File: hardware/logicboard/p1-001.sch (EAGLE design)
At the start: 27 parts, among them IC1 74LS07N

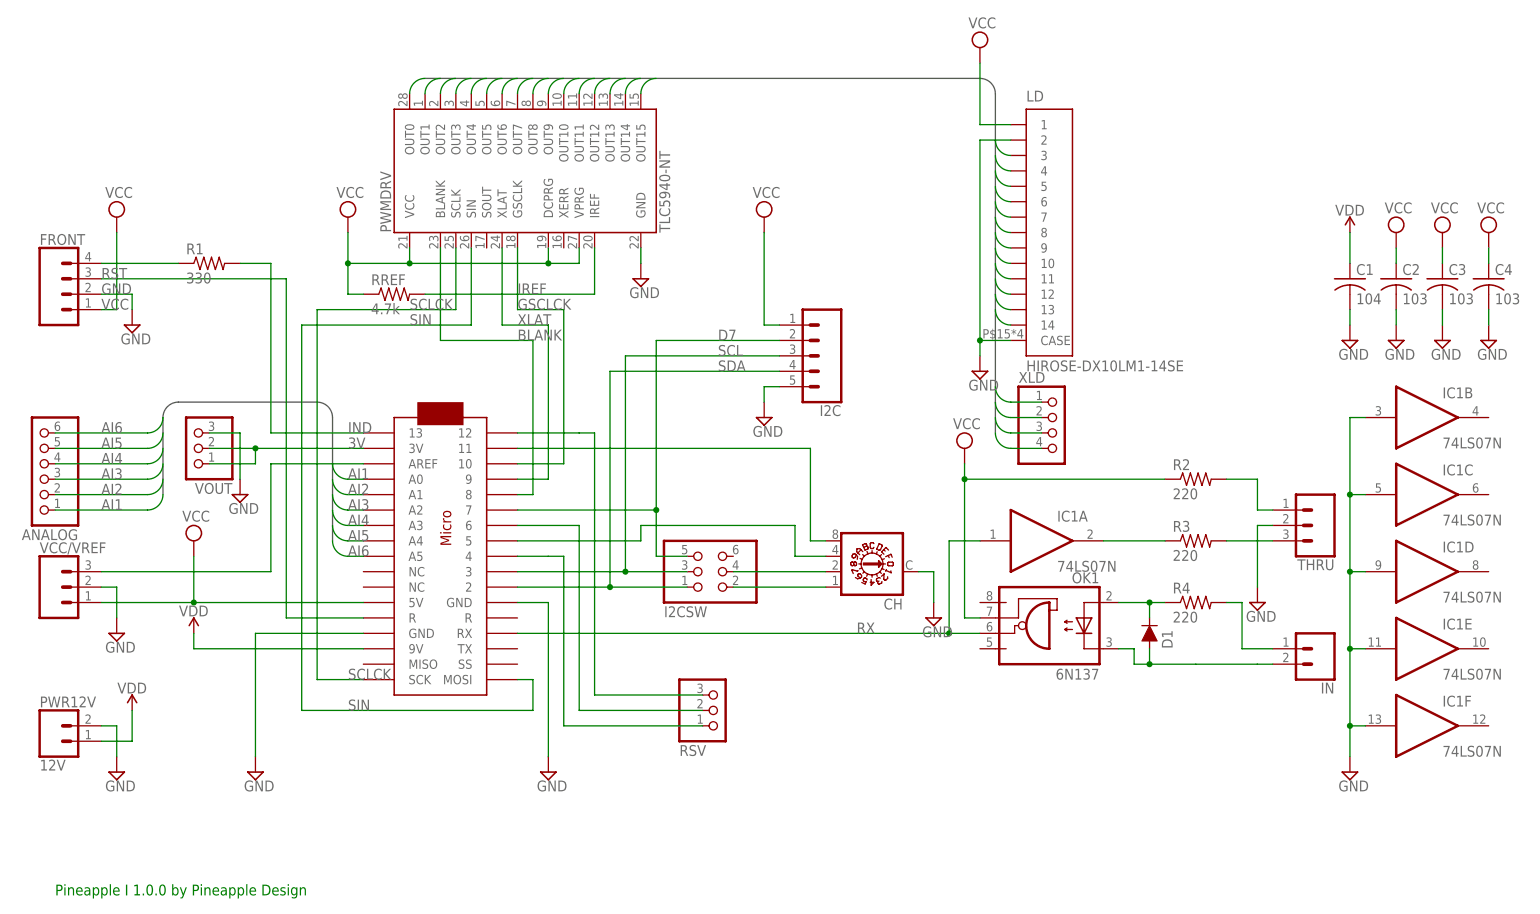
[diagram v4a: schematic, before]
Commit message: I2C pull-up.
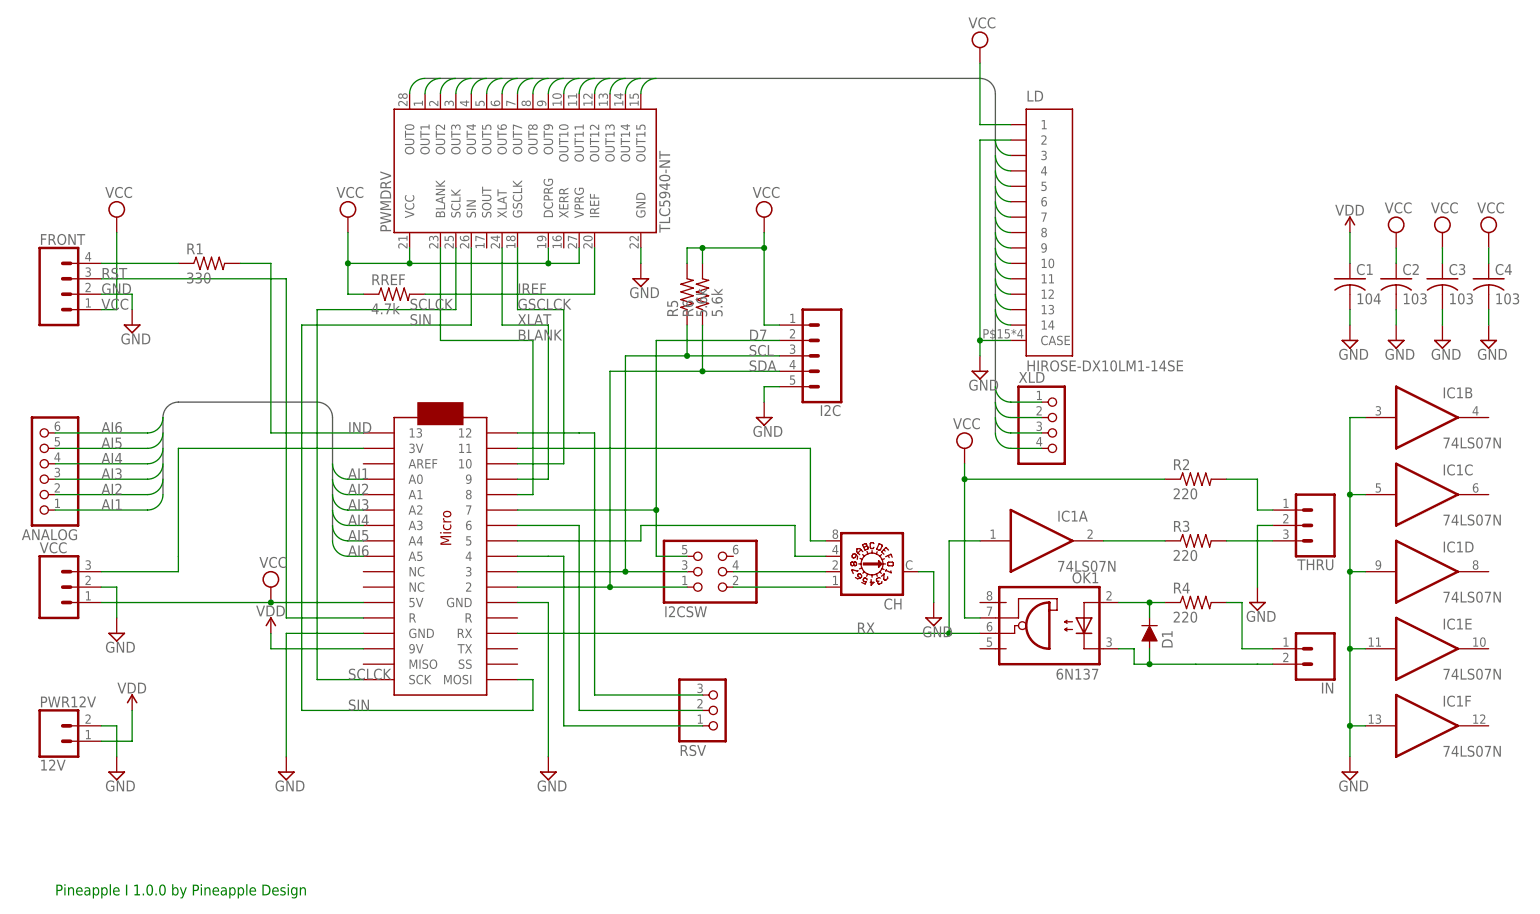
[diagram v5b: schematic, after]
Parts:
- removed VOUT: (no value), pinhead:PINHD-1X3
- added R5, R6: 5.6k, resistor:R-US_0204/5
- renumbered VCC/VREF to VCC
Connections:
- removed net 3V: U$1.3V, VOUT.1, VOUT.2
- removed net VREF: U$1.AREF, VCC.3
- new net V3V: U$1.3V, VCC.3
- net GND: no longer VOUT.3
- net SCL: now also R5.1
- net SDA: now also R6.1
- net VCC: now also R5.2, R6.2
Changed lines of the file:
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@@
 <setting verticaltext="up"/>
 </settings>
-<grid distance="0.1" unitdist="inch" unit="inch" style="lines" multiple="1" display="no" altdistance="0.01" altunitdist="inch" altunit="inch"/>
+<grid distance="0.1" unitdist="inch" unit="inch" style="dots" multiple="1" display="yes" altdistance="0.01" altunitdist="inch" altunit="inch"/>
 <layers>
 <layer number="1" name="Top" color="4" fill="1" visible="no" active="no"/>
@@
 <part name="SUPPLY8" library="supply2" library_urn="urn:adsk.eagle:library:372" deviceset="VCC" device=""/>
 <part name="SUPPLY15" library="supply2" library_urn="urn:adsk.eagle:library:372" deviceset="GND" device=""/>
-<part name="VOUT" library="pinhead" library_urn="urn:adsk.eagle:library:325" deviceset="PINHD-1X3" device="" package3d_urn="urn:adsk.eagle:package:22458/2"/>
-<part name="$1_39_$_2018-07-15_07-03-01" library="supply2" library_urn="urn:adsk.eagle:library:372" deviceset="GND" device=""/>
-<part name="VCC/VREF" library="SparkFun-Connectors" library_urn="urn:adsk.eagle:library:513" deviceset="CONN_03" device="JST-PTH-VERT" package3d_urn="urn:adsk.eagle:package:38080/1"/>
+<part name="VCC" library="SparkFun-Connectors" library_urn="urn:adsk.eagle:library:513" deviceset="CONN_03" device="JST-PTH-VERT" package3d_urn="urn:adsk.eagle:package:38080/1"/>
 <part name="$1_52_$_2018-07-15_07-03-01" library="supply2" library_urn="urn:adsk.eagle:library:372" deviceset="GND" device=""/>
+<part name="R5" library="resistor" library_urn="urn:adsk.eagle:library:348" deviceset="R-US_" device="0204/5" package3d_urn="urn:adsk.eagle:package:25955/1" value="5.6k"/>
+<part name="R6" library="resistor" library_urn="urn:adsk.eagle:library:348" deviceset="R-US_" device="0204/5" package3d_urn="urn:adsk.eagle:package:25955/1" value="5.6k"/>
 </parts>
 <sheets>
@@
 <instance part="IC1" gate="C" x="226.06" y="66.04"/>
 <instance part="D1" gate="G$1" x="180.34" y="43.18" rot="MR90"/>
-<instance part="SUPPLY14" gate="G$1" x="22.86" y="58.42"/>
-<instance part="$1_39_$_2018-07-15_07-03-06" gate="GND" x="33.02" y="20.32"/>
+<instance part="SUPPLY14" gate="G$1" x="35.56" y="50.8"/>
+<instance part="$1_39_$_2018-07-15_07-03-06" gate="GND" x="38.1" y="20.32"/>
 <instance part="IN" gate="G$1" x="208.28" y="40.64" rot="R180"/>
 <instance part="THRU" gate="J$1" x="208.28" y="60.96" rot="R180"/>
@@
 <instance part="PWR12V" gate="G$1" x="0" y="25.4"/>
 <instance part="$1_51_$_2018-07-15_07-03-06" gate="VDD" x="12.7" y="30.48"/>
-<instance part="SUPPLY12" gate="VDD" x="22.86" y="43.18"/>
+<instance part="SUPPLY12" gate="VDD" x="35.56" y="43.18"/>
 <instance part="$1_52_$_2018-07-15_07-03-06" gate="GND" x="10.16" y="20.32"/>
 <instance part="FRONT" gate="G$1" x="2.54" y="99.06"/>
@@
 <instance part="SUPPLY8" gate="G$1" x="116.84" y="111.76"/>
 <instance part="SUPPLY15" gate="GND" x="116.84" y="78.74"/>
-<instance part="VOUT" gate="A" x="22.86" y="73.66" rot="R180"/>
-<instance part="$1_39_$_2018-07-15_07-03-01" gate="GND" x="30.48" y="66.04"/>
-<instance part="VCC/VREF" gate="J$1" x="0" y="50.8"/>
+<instance part="VCC" gate="J$1" x="0" y="50.8"/>
 <instance part="$1_52_$_2018-07-15_07-03-01" gate="GND" x="10.16" y="43.18"/>
+<instance part="R5" gate="G$1" x="104.14" y="99.06" rot="R90"/>
+<instance part="R6" gate="G$1" x="106.68" y="99.06" rot="R90"/>
 </instances>
 <busses>
@@
 </segment>
 <segment>
-<wire x1="50.8" y1="43.18" x2="33.02" y2="43.18" width="0.1524" layer="91"/>
+<wire x1="50.8" y1="43.18" x2="38.1" y2="43.18" width="0.1524" layer="91"/>
 <pinref part="$1_39_$_2018-07-15_07-03-06" gate="GND" pin="GND"/>
-<wire x1="33.02" y1="43.18" x2="33.02" y2="22.86" width="0.1524" layer="91"/>
+<wire x1="38.1" y1="43.18" x2="38.1" y2="22.86" width="0.1524" layer="91"/>
 <pinref part="U$1" gate="G$1" pin="GND"/>
 </segment>
@@
 </segment>
 <segment>
-<pinref part="VOUT" gate="A" pin="3"/>
-<wire x1="25.4" y1="76.2" x2="30.48" y2="76.2" width="0.1524" layer="91"/>
-<pinref part="$1_39_$_2018-07-15_07-03-01" gate="GND" pin="GND"/>
-<wire x1="30.48" y1="76.2" x2="30.48" y2="68.58" width="0.1524" layer="91"/>
-</segment>
-<segment>
-<pinref part="VCC/VREF" gate="J$1" pin="2"/>
+<pinref part="VCC" gate="J$1" pin="2"/>
 <wire x1="7.62" y1="50.8" x2="10.16" y2="50.8" width="0.1524" layer="91"/>
 <pinref part="$1_52_$_2018-07-15_07-03-01" gate="GND" pin="GND"/>
@@
 <segment>
 <pinref part="SUPPLY14" gate="G$1" pin="VCC"/>
-<wire x1="22.86" y1="55.88" x2="22.86" y2="48.26" width="0.1524" layer="91"/>
 <pinref part="U$1" gate="G$1" pin="5V"/>
-<wire x1="22.86" y1="48.26" x2="50.8" y2="48.26" width="0.1524" layer="91"/>
-<pinref part="VCC/VREF" gate="J$1" pin="1"/>
-<wire x1="22.86" y1="48.26" x2="7.62" y2="48.26" width="0.1524" layer="91"/>
-<junction x="22.86" y="48.26"/>
+<wire x1="35.56" y1="48.26" x2="50.8" y2="48.26" width="0.1524" layer="91"/>
+<pinref part="VCC" gate="J$1" pin="1"/>
+<wire x1="35.56" y1="48.26" x2="7.62" y2="48.26" width="0.1524" layer="91"/>
+<junction x="35.56" y="48.26"/>
 </segment>
 <segment>
@@
 <segment>
 <pinref part="SUPPLY8" gate="G$1" pin="VCC"/>
-<wire x1="116.84" y1="109.22" x2="116.84" y2="93.98" width="0.1524" layer="91"/>
+<wire x1="116.84" y1="109.22" x2="116.84" y2="106.68" width="0.1524" layer="91"/>
 <pinref part="I2C" gate="G$1" pin="1"/>
+<wire x1="116.84" y1="106.68" x2="116.84" y2="93.98" width="0.1524" layer="91"/>
 <wire x1="116.84" y1="93.98" x2="119.38" y2="93.98" width="0.1524" layer="91"/>
+<pinref part="R5" gate="G$1" pin="2"/>
+<wire x1="104.14" y1="104.14" x2="104.14" y2="106.68" width="0.1524" layer="91"/>
+<wire x1="104.14" y1="106.68" x2="106.68" y2="106.68" width="0.1524" layer="91"/>
+<junction x="116.84" y="106.68"/>
+<pinref part="R6" gate="G$1" pin="2"/>
+<wire x1="106.68" y1="106.68" x2="116.84" y2="106.68" width="0.1524" layer="91"/>
+<wire x1="106.68" y1="104.14" x2="106.68" y2="106.68" width="0.1524" layer="91"/>
+<junction x="106.68" y="106.68"/>
 </segment>
 </net>
@@
 <segment>
 <pinref part="SUPPLY12" gate="VDD" pin="VDD"/>
-<wire x1="22.86" y1="43.18" x2="22.86" y2="40.64" width="0.1524" layer="91"/>
-<wire x1="22.86" y1="40.64" x2="50.8" y2="40.64" width="0.1524" layer="91"/>
+<wire x1="35.56" y1="43.18" x2="35.56" y2="40.64" width="0.1524" layer="91"/>
+<wire x1="35.56" y1="40.64" x2="50.8" y2="40.64" width="0.1524" layer="91"/>
 <pinref part="U$1" gate="G$1" pin="9V"/>
 </segment>
@@
 <junction x="91.44" y="50.8"/>
 <pinref part="I2C" gate="G$1" pin="4"/>
-<wire x1="91.44" y1="86.36" x2="119.38" y2="86.36" width="0.1524" layer="91"/>
-<label x="109.22" y="86.36" size="1.778" layer="95"/>
+<wire x1="91.44" y1="86.36" x2="106.68" y2="86.36" width="0.1524" layer="91"/>
+<label x="114.3" y="86.36" size="1.778" layer="95"/>
+<pinref part="R6" gate="G$1" pin="1"/>
+<wire x1="106.68" y1="86.36" x2="119.38" y2="86.36" width="0.1524" layer="91"/>
+<wire x1="106.68" y1="93.98" x2="106.68" y2="86.36" width="0.1524" layer="91"/>
+<junction x="106.68" y="86.36"/>
 </segment>
 </net>
@@
 <junction x="93.98" y="53.34"/>
 <pinref part="I2C" gate="G$1" pin="3"/>
-<wire x1="93.98" y1="88.9" x2="119.38" y2="88.9" width="0.1524" layer="91"/>
-<label x="109.22" y="88.9" size="1.778" layer="95"/>
+<wire x1="93.98" y1="88.9" x2="104.14" y2="88.9" width="0.1524" layer="91"/>
+<label x="114.3" y="88.9" size="1.778" layer="95"/>
+<pinref part="R5" gate="G$1" pin="1"/>
+<wire x1="104.14" y1="88.9" x2="119.38" y2="88.9" width="0.1524" layer="91"/>
+<wire x1="104.14" y1="93.98" x2="104.14" y2="88.9" width="0.1524" layer="91"/>
+<junction x="104.14" y="88.9"/>
 </segment>
 </net>
@@
 <wire x1="99.06" y1="63.5" x2="99.06" y2="91.44" width="0.1524" layer="91"/>
 <junction x="99.06" y="63.5"/>
-<label x="109.22" y="91.44" size="1.778" layer="95"/>
+<label x="114.3" y="91.44" size="1.778" layer="95"/>
 </segment>
 </net>
@@
 </segment>
 </net>
-<net name="3V" class="0">
+<net name="V3V" class="0">
 <segment>
 <pinref part="U$1" gate="G$1" pin="3V"/>
-<wire x1="50.8" y1="73.66" x2="33.02" y2="73.66" width="0.1524" layer="91"/>
-<wire x1="33.02" y1="73.66" x2="25.4" y2="73.66" width="0.1524" layer="91"/>
-<wire x1="33.02" y1="73.66" x2="33.02" y2="71.12" width="0.1524" layer="91"/>
-<junction x="33.02" y="73.66"/>
-<wire x1="33.02" y1="71.12" x2="25.4" y2="71.12" width="0.1524" layer="91"/>
-<pinref part="VOUT" gate="A" pin="1"/>
-<pinref part="VOUT" gate="A" pin="2"/>
-<label x="48.26" y="73.66" size="1.778" layer="95"/>
-</segment>
-</net>
-<net name="VREF" class="0">
-<segment>
-<pinref part="U$1" gate="G$1" pin="AREF"/>
-<wire x1="50.8" y1="71.12" x2="35.56" y2="71.12" width="0.1524" layer="91"/>
-<wire x1="35.56" y1="71.12" x2="35.56" y2="53.34" width="0.1524" layer="91"/>
-<pinref part="VCC/VREF" gate="J$1" pin="3"/>
-<wire x1="35.56" y1="53.34" x2="7.62" y2="53.34" width="0.1524" layer="91"/>
-</segment>
-</net>
+<wire x1="50.8" y1="73.66" x2="20.32" y2="73.66" width="0.1524" layer="91"/>
+<wire x1="20.32" y1="73.66" x2="20.32" y2="55.88" width="0.1524" layer="91"/>
+<wire x1="20.32" y1="55.88" x2="20.32" y2="53.34" width="0.1524" layer="91"/>
+<pinref part="VCC" gate="J$1" pin="3"/>
+<wire x1="20.32" y1="53.34" x2="7.62" y2="53.34" width="0.1524" layer="91"/>
+</segment>
+</net>

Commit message: Layout.
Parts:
- removed ANALOG: (no value), pinhead:PINHD-1X6
- removed CH: (no value), switch-dil:A1353HEX
- removed I2CSW: (no value), pinhead:PINHD-2X3
- removed XLD: (no value), pinhead:PINHD-1X4
- RSV: device pinhead:PINHD-1X3 -> pinhead:PINHD-1X5
- renumbered LD to LIGHTDRIVE
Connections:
- net RSV1 renamed N$1
- removed net AI1: ANALOG.1, U$1.A0
- removed net AI2: ANALOG.2, U$1.A1
- removed net AI3: ANALOG.3, U$1.A2
- removed net AI4: ANALOG.4, U$1.A3
- removed net AI5: ANALOG.5, U$1.A4
- removed net AI6: ANALOG.6, U$1.A5
- removed net LD13: PWMDRV.OUT12, XLD.1
- removed net LD14: PWMDRV.OUT13, XLD.2
- removed net LD15: PWMDRV.OUT14, XLD.3
- removed net LD16: PWMDRV.OUT15, XLD.4
- removed net RSV2: RSV.2, U$1.6
- removed net RSV3: RSV.3, U$1.12
- removed net SW1: CH.1, I2CSW.2
- removed net SW2: CH.2, I2CSW.4
- removed net SW4: CH.4, U$1.5
- removed net SW8: CH.8, U$1.11
- new net N$4: RSV.2, U$1.5
- new net N$6: RSV.3, U$1.6
- new net N$7: RSV.4, U$1.11
- new net N$8: RSV.5, U$1.12
- net D7: no longer I2CSW.5
- net GND: no longer CH.C
- net SCL: no longer I2CSW.3
- net SDA: no longer I2CSW.1

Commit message: New layout.
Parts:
- removed C4: 103, rcl:C-US025-025X050
- RREF: device resistor:R-US_0204/5 -> pinhead:PINHD-1X2
- RSV: device pinhead:PINHD-1X5 -> SparkFun-Connectors:CONN_05JST-VERT
- VCC: device SparkFun-Connectors:CONN_03JST-PTH-VERT -> SparkFun-Connectors:CONN_03JST-PTH
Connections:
- net GND: no longer C4.2
- net VCC: no longer C4.1
